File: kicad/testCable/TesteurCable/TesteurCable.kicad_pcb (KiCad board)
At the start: 2 copper layers, 45 x 35 mm, 7 parts, among them J1 Conn_01x02_Male, J2 Conn_01x02_Female, J3 Conn_01x02_Male, J4 Conn_01x02_Female

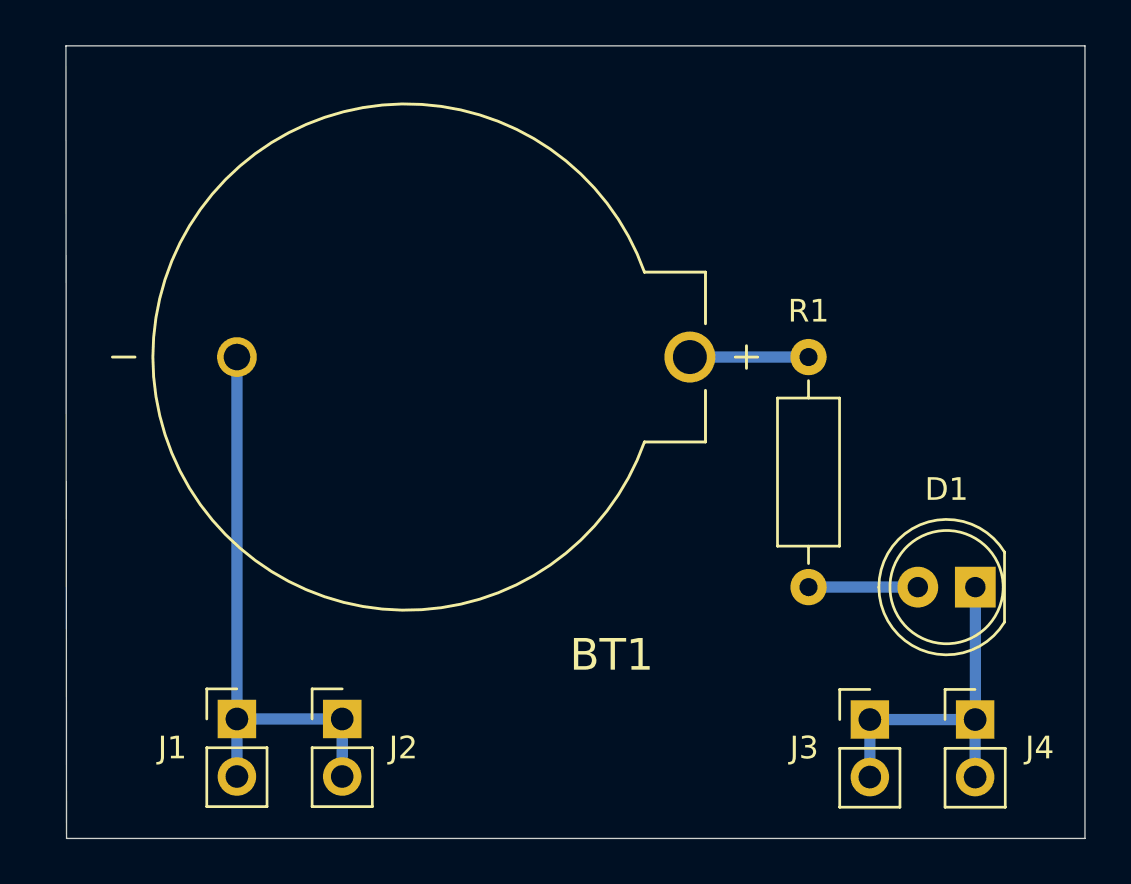
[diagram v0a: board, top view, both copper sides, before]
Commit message: Modify the schema of Testeur de cable.
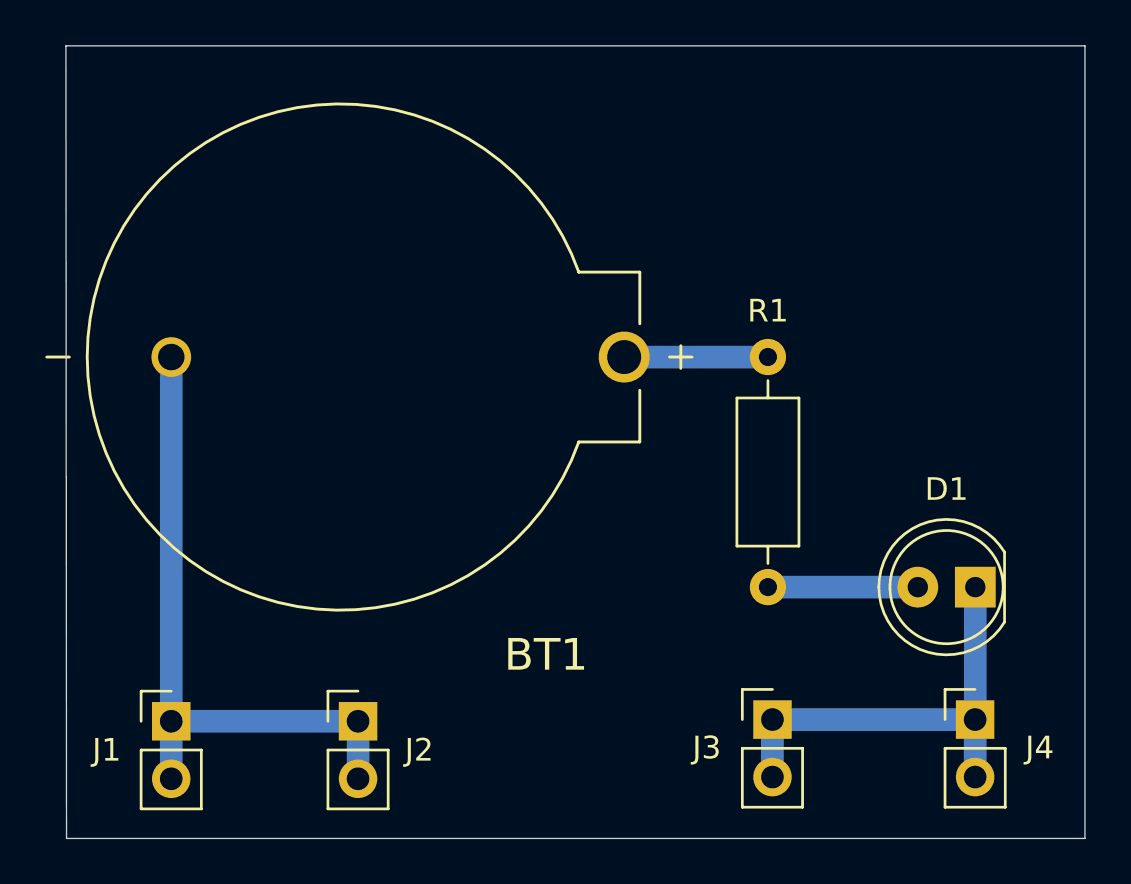
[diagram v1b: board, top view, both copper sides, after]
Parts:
- moved J3 4.30 mm to (48.7, 47.3)
- moved J1 2.90 mm to (22.2, 47.3)
- moved BT1 2.90 mm to (32.2, 31.2)
- moved R1 1.79 mm to (48.5, 41.4)
- moved J2 0.71 mm to (30.4, 47.3)
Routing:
- net Net-(D1-Pad1): track 15.6 -> 19.9 mm
- net Net-(BT1-Pad-): track 25.7 -> 29.3 mm
- net Net-(D1-Pad2): track 4.83 -> 6.62 mm
- net Net-(BT1-Pad+): track 5.24 -> 6.35 mm
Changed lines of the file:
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@@
     (thickness 1.6)
     (drawings 4)
-    (tracks 12)
+    (tracks 14)
     (zones 0)
     (modules 7)
@@
     (pcbplotparams
       (layerselection 0x01000_fffffffe)
-      (usegerberextensions false)
+      (usegerberextensions true)
       (usegerberattributes true)
       (usegerberadvancedattributes true)
@@
       (drillshape 0)
       (scaleselection 1)
-      (outputdirectory "gerber"))
+      (outputdirectory "gerber_1"))
   )
   (net 0 "")
@@
   )
   (module battery_holder:BAT_BS-7 (layer F.Cu)
-    (at 35.052 31.242)
+    (at 32.152 31.242)
     (fp_text reference BT1 (at 6.548 13.158) (layer F.SilkS)
       (effects (font (size 1.4 1.4) (thickness 0.15)))
@@
   )
   (module Resistor_THT:R_Axial_DIN0207_L6.3mm_D2.5mm_P10.16mm_Horizontal (layer F.Cu)
-    (at 50.292 41.402 90)
+    (at 48.5 41.4 90)
     (descr "Resistor, Axial_DIN0207 series, Axial, Horizontal, pin pitch=10.16mm, 0.25W = 1/4W, length*diameter=6.3*2.5mm^2, http://cdn-reichelt.de/documents/datenblatt/B400/1_4W%23YAG.pdf")
     (tags "Resistor Axial_DIN0207 series Axial Horizontal pin pitch 10.16mm 0.25W = 1/4W length 6.3mm diameter 2.5mm")
@@
   )
   (module Connector_PinHeader_2.54mm:PinHeader_1x02_P2.54mm_Vertical (layer F.Cu)
-    (at 25.050001 47.225001)
+    (at 22.150001 47.325001)
     (descr "Through hole straight pin header, 1x02, 2.54mm pitch, single row")
     (tags "Through hole pin header THT 1x02 2.54mm single row")
@@
   )
   (module Connector_PinHeader_2.54mm:PinHeader_1x02_P2.54mm_Vertical (layer F.Cu)
-    (at 29.700001 47.225001)
+    (at 30.400001 47.325001)
     (descr "Through hole straight pin header, 1x02, 2.54mm pitch, single row")
     (tags "Through hole pin header THT 1x02 2.54mm single row")
@@
     )
     (fp_text value Conn_01x02_Female (at 0 4.87) (layer F.Fab)
-      (effects (font (size 1 1) (thickness 0.15)))
-    )
-    (fp_text user %R (at 0 1.27 90) (layer F.Fab)
       (effects (font (size 1 1) (thickness 0.15)))
     )
@@
     (fp_line (start 1.8 4.35) (end 1.8 -1.8) (layer F.CrtYd) (width 0.05))
     (fp_line (start 1.8 -1.8) (end -1.8 -1.8) (layer F.CrtYd) (width 0.05))
+    (fp_text user %R (at 0 1.27 90) (layer F.Fab)
+      (effects (font (size 1 1) (thickness 0.15)))
+    )
     (pad 2 thru_hole oval (at 0 2.54) (size 1.7 1.7) (drill 1) (layers *.Cu *.Mask)
       (net 3 "Net-(BT1-Pad-)"))
@@
   )
   (module Connector_PinHeader_2.54mm:PinHeader_1x02_P2.54mm_Vertical (layer F.Cu)
-    (at 53.000001 47.250001)
+    (at 48.700001 47.250001)
     (descr "Through hole straight pin header, 1x02, 2.54mm pitch, single row")
     (tags "Through hole pin header THT 1x02 2.54mm single row")
@@
       (effects (font (size 1 1) (thickness 0.15)))
     )
-    (fp_text user %R (at 0 1.27 90) (layer F.Fab)
-      (effects (font (size 1 1) (thickness 0.15)))
-    )
     (fp_line (start -0.635 -1.27) (end 1.27 -1.27) (layer F.Fab) (width 0.1))
     (fp_line (start 1.27 -1.27) (end 1.27 3.81) (layer F.Fab) (width 0.1))
@@
     (fp_line (start 1.8 4.35) (end 1.8 -1.8) (layer F.CrtYd) (width 0.05))
     (fp_line (start 1.8 -1.8) (end -1.8 -1.8) (layer F.CrtYd) (width 0.05))
+    (fp_text user %R (at 0 1.27 90) (layer F.Fab)
+      (effects (font (size 1 1) (thickness 0.15)))
+    )
     (pad 2 thru_hole oval (at 0 2.54) (size 1.7 1.7) (drill 1) (layers *.Cu *.Mask)
       (net 2 "Net-(D1-Pad1)"))
@@
   (gr_line (start 62.5 17.5) (end 62.5 52.5) (layer Edge.Cuts) (width 0.05))
   (gr_line (start 17.5 17.5) (end 62.5 17.5) (layer Edge.Cuts) (width 0.05))
-  (segment (start 50.292 41.402) (end 55.118 41.402) (width 0.5) (layer B.Cu) (net 1))
+  (segment (start 48.502 41.402) (end 55.118 41.402) (width 1) (layer B.Cu) (net 1))
+  (segment (start 48.5 41.4) (end 48.502 41.402) (width 0.5) (layer B.Cu) (net 1))
   (segment (start 57.658 47.242002) (end 57.650001 47.250001) (width 0.5) (layer F.Cu) (net 2))
-  (segment (start 57.658 41.402) (end 57.658 47.242002) (width 0.5) (layer B.Cu) (net 2))
-  (segment (start 57.650001 47.250001) (end 53.000001 47.250001) (width 0.5) (layer B.Cu) (net 2))
-  (segment (start 53.000001 47.250001) (end 53.000001 49.790001) (width 0.5) (layer B.Cu) (net 2))
-  (segment (start 57.650001 47.250001) (end 57.650001 49.790001) (width 0.5) (layer B.Cu) (net 2))
-  (segment (start 25.052 47.223002) (end 25.050001 47.225001) (width 0.5) (layer F.Cu) (net 3))
-  (segment (start 25.052 31.242) (end 25.052 47.223002) (width 0.5) (layer B.Cu) (net 3))
-  (segment (start 25.050001 47.225001) (end 25.050001 49.765001) (width 0.5) (layer B.Cu) (net 3))
-  (segment (start 25.050001 47.225001) (end 29.700001 47.225001) (width 0.5) (layer B.Cu) (net 3))
-  (segment (start 29.700001 47.225001) (end 29.700001 49.765001) (width 0.5) (layer B.Cu) (net 3))
-  (segment (start 45.052 31.242) (end 50.292 31.242) (width 0.5) (layer B.Cu) (net 4))
+  (segment (start 57.658 41.402) (end 57.658 47.242002) (width 1) (layer B.Cu) (net 2))
+  (segment (start 48.700001 47.250001) (end 48.700001 49.790001) (width 1) (layer B.Cu) (net 2))
+  (segment (start 57.650001 47.250001) (end 57.650001 49.790001) (width 1) (layer B.Cu) (net 2))
+  (segment (start 57.650001 47.250001) (end 48.700001 47.250001) (width 1) (layer B.Cu) (net 2))
+  (segment (start 22.152 47.323002) (end 22.150001 47.325001) (width 0.5) (layer F.Cu) (net 3))
+  (segment (start 22.150001 47.325001) (end 22.150001 49.865001) (width 1) (layer B.Cu) (net 3))
+  (segment (start 30.400001 47.325001) (end 30.400001 49.865001) (width 1) (layer B.Cu) (net 3))
+  (segment (start 22.152 31.242) (end 22.152 47.223002) (width 1) (layer B.Cu) (net 3))
+  (segment (start 22.150001 47.325001) (end 30.400001 47.325001) (width 1) (layer B.Cu) (net 3))
+  (segment (start 48.498 31.242) (end 48.5 31.24) (width 0.5) (layer B.Cu) (net 4))
+  (segment (start 42.152 31.242) (end 48.498 31.242) (width 1) (layer B.Cu) (net 4))
 )
